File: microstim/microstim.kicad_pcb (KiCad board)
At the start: 2 copper layers, 196.1 x 76.2 mm, 75 parts, among them J1 Conn_Coaxial, J10 Conn_Coaxial, J11 Screw_Terminal_01x02, J12 Conn_Coaxial, J2 Conn_Coaxial, J3 Screw_Terminal_01x02, J4 Screw_Terminal_01x02, J5 Conn_Coaxial, J6 Conn_Coaxial, J7 Screw_Terminal_01x02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

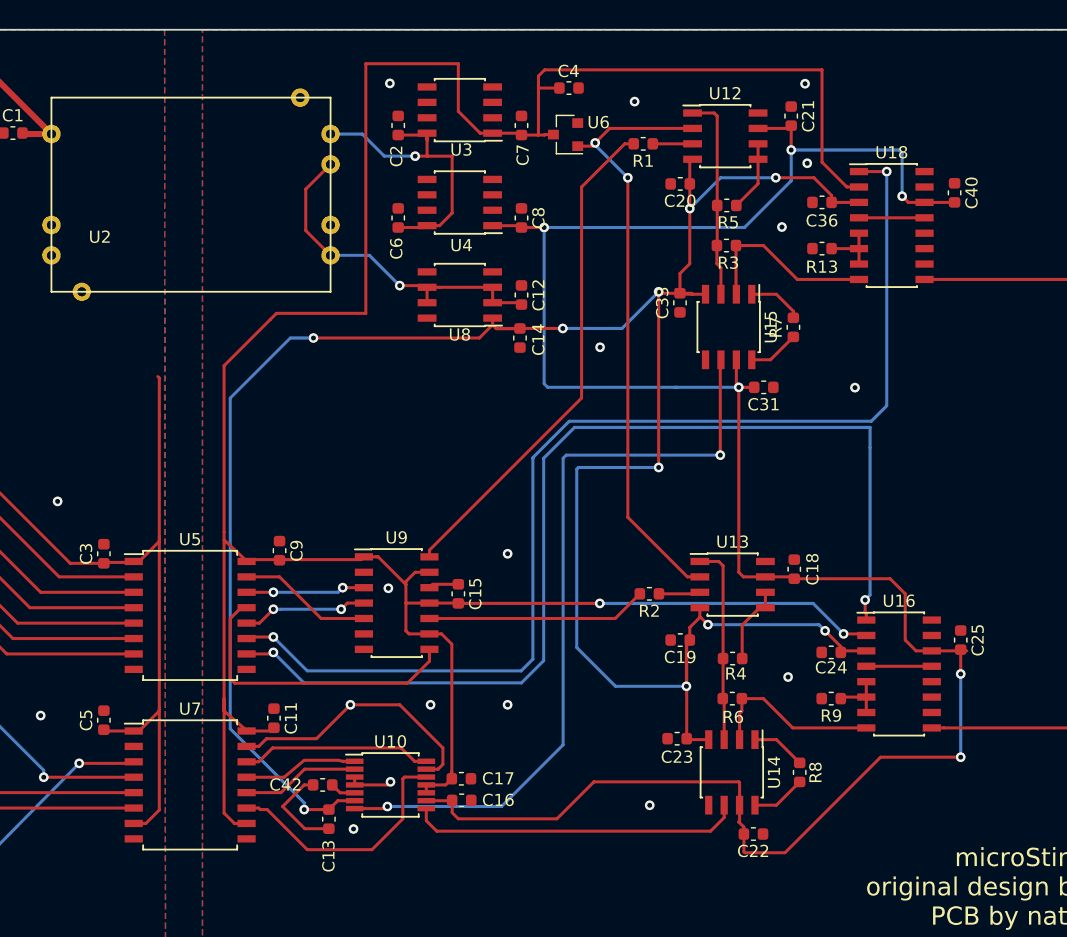
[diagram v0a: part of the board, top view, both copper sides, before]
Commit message: replaced LT1167 with INA826 instrument amp. hopefully this wasn't a terrible decision.
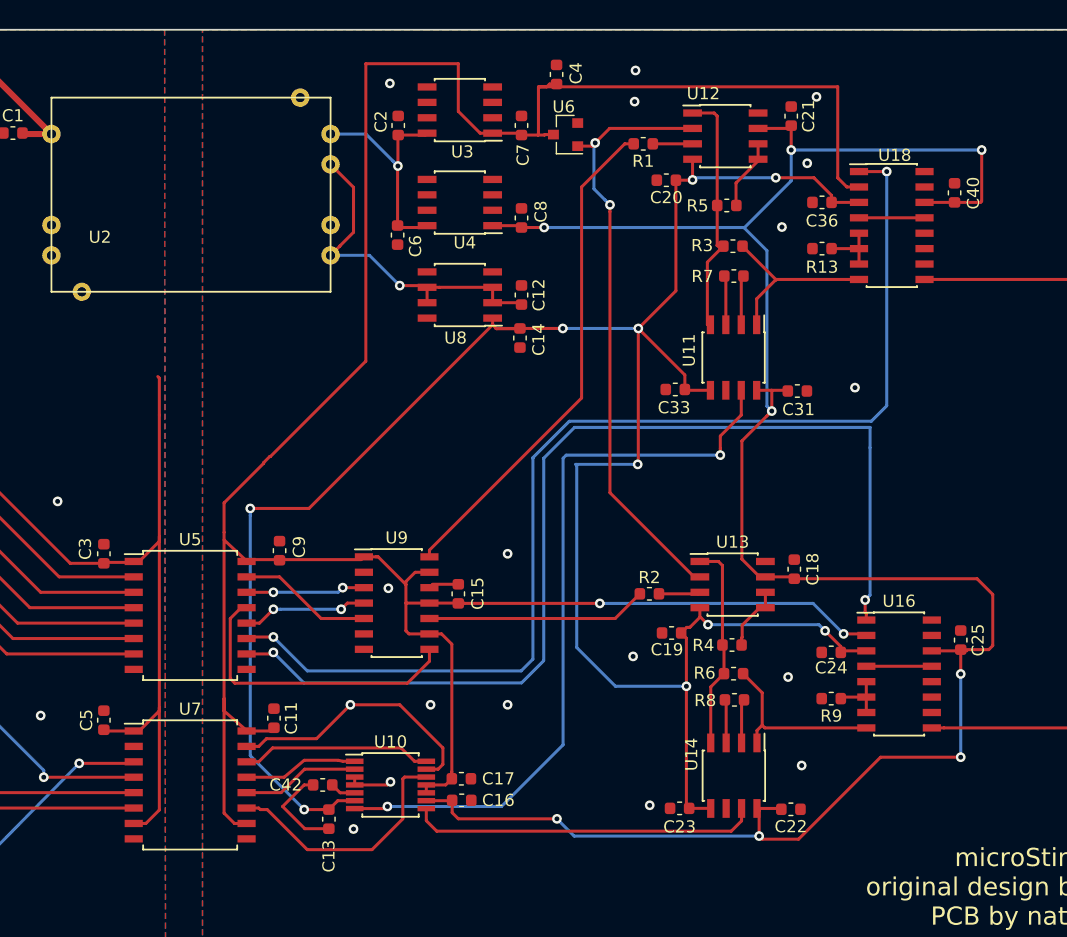
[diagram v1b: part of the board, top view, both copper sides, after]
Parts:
- removed U15: LT1167, Package_SO:SOIC-8_3.9x4.9mm_P1.27mm
- added U11: INA826, Package_SO:SOIC-8_3.9x4.9mm_P1.27mm, F.Cu at (192.1, 48.6)
- U14: value LT1167 -> INA826
- U3: value L78L05_SO8 -> L78L05
- U4: value L78L12_SO8 -> L78L12
- U8: value L79L12_SO8 -> L79L12
- moved R8 8.04 mm to (192.2, 76.8), turned to 0 degrees
- moved C33 7.15 mm to (187.3, 51.2), turned to 0 degrees
- moved R7 6.47 mm to (192.1, 41.9), turned to 0 degrees
- moved C23 5.74 mm to (187.7, 85.8)
- moved C22 3.70 mm to (196.8, 85.8)
- moved C31 2.79 mm to (197.4, 51.4)
- moved R6 2.06 mm to (192.1, 74.7)
- moved C4 1.51 mm to (177.5, 25.3), turned to 270 degrees
- moved C6 1.41 mm to (164.4, 38.5), turned to 90 degrees
- moved C20 1.18 mm to (186.6, 34.0)
- moved R4 1.12 mm to (192.0, 72.3)
- moved C19 0.92 mm to (187.0, 71.3)
- moved R3 0.54 mm to (192.0, 39.4)
- moved U14 0.32 mm to (192.1, 83.1)
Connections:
- U14 pad 1: Net-(R8-Pad2) -> Net-(R6-Pad2)
- U14 pad 2: Net-(R6-Pad2) -> Net-(R8-Pad2)
- U14 pad 3: Net-(R4-Pad1) -> Net-(R8-Pad1)
- U14 pad 4: -12V -> Net-(R4-Pad1)
- U14 pad 5: GNDREF -> -12V
- U14 pad 6: ISENSE1 -> GNDREF
- U14 pad 7: +12V -> ISENSE1
- U14 pad 8: Net-(R8-Pad1) -> +12V
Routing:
- net +12V: track 187.8 -> 203.3 mm, vias 6 -> 8
- net +5V: track 222.2 -> 215.9 mm
- net +15V: track 25.1 -> 19.1 mm
- net -12V: track 194.1 -> 189.1 mm
- net Net-(R3-Pad1): track 17.0 -> 20.6 mm
- net ISENSE0: track 63.9 -> 62.1 mm
- net ISENSE1: track 27.4 -> 28.7 mm
- net Net-(R4-Pad2): track 6.53 -> 5.43 mm
- net Net-(R8-Pad2): track 4.48 -> 3.63 mm
- net Net-(R8-Pad1): track 4.48 -> 3.75 mm
- net Net-(R4-Pad1): track 16.4 -> 17.1 mm
- net GNDREF: vias 17 -> 19
